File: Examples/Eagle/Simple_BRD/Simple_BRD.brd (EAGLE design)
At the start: 33.7 x 26.7 mm, 6 parts

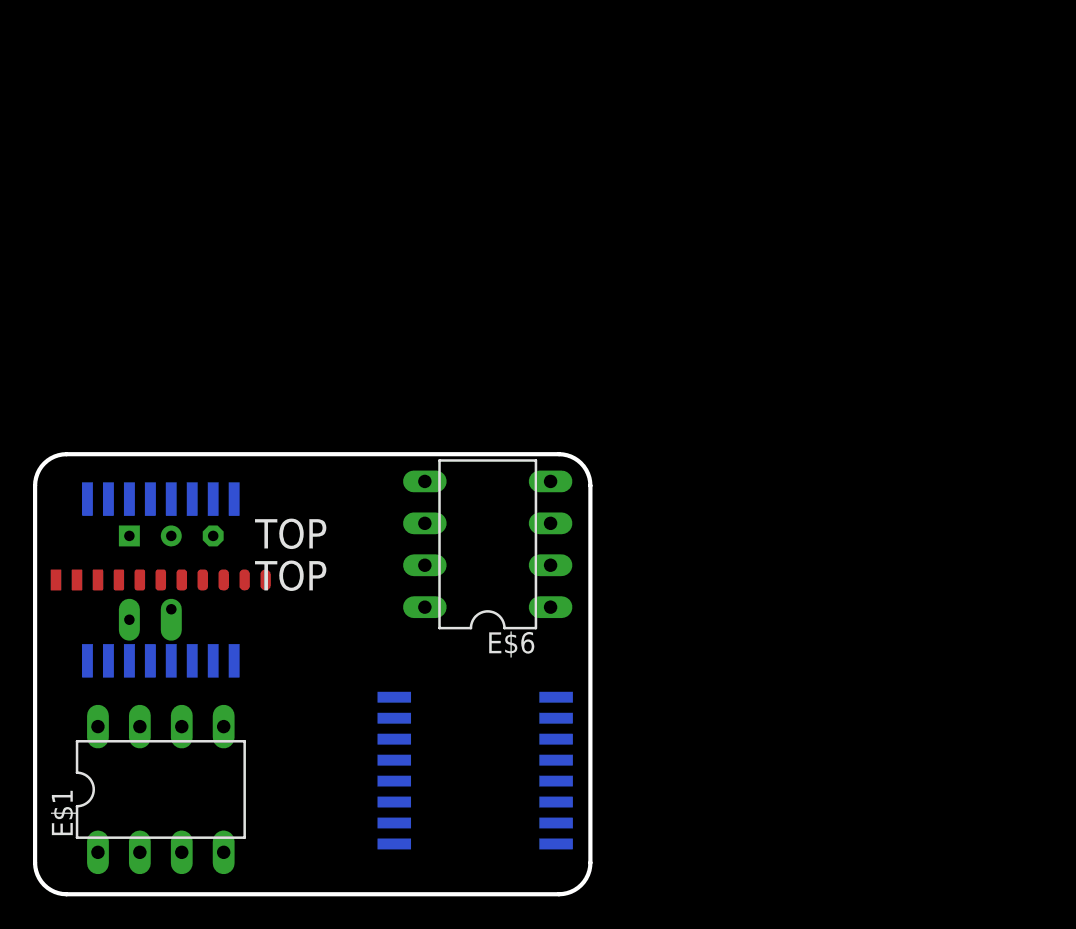
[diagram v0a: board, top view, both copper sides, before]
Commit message: Created new PCB in EagleCAD that utilizes most export features
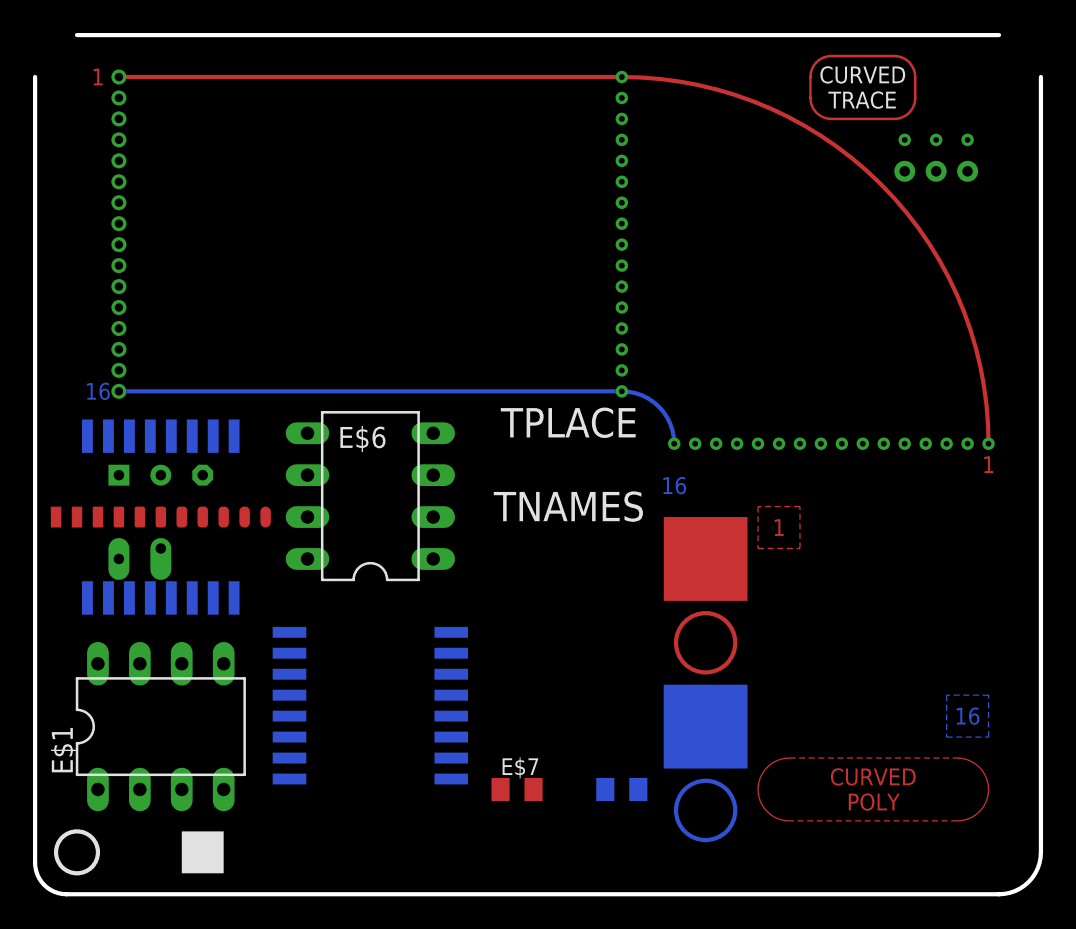
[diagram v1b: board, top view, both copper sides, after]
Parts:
- added E$7, E$8: 1uF, adafruit:C0805K
- moved E$6 7.69 mm to (20.3, 24.1)
- moved E$5 7.47 mm to (20.3, 11.4)
- moved E$1 3.81 mm to (7.62, 10.2)
- moved E$2 3.81 mm to (7.62, 22.9)
- moved E$4 3.81 mm to (7.62, 22.9)
- moved E$3 3.74 mm to (5.08, 25.4)
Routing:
- net S$1: track 0.00 -> 61.9 mm, vias 0 -> 3
- net S$2: track 0.00 -> 60.1 mm, vias 0 -> 3
- net S$4: track 0.00 -> 58.3 mm, vias 0 -> 3
- net S$5: track 0.00 -> 56.5 mm, vias 0 -> 3
- net S$6: track 0.00 -> 54.7 mm, vias 0 -> 3
- net S$7: track 0.00 -> 52.9 mm, vias 0 -> 3
- net S$8: track 0.00 -> 51.1 mm, vias 0 -> 3
- net S$9: track 0.00 -> 49.3 mm, vias 0 -> 3
- net S$10: track 0.00 -> 47.5 mm, vias 0 -> 3
- net S$11: track 0.00 -> 45.7 mm, vias 0 -> 3
- net S$13: track 0.00 -> 44.0 mm, vias 0 -> 3
- net S$12: track 0.00 -> 42.2 mm, vias 0 -> 3
- net S$14: track 0.00 -> 40.4 mm, vias 0 -> 3
- net S$15: track 0.00 -> 38.6 mm, vias 0 -> 3
- net S$16: track 0.00 -> 36.8 mm, vias 0 -> 3
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- added copper zone on layer 1, net TEST
- added copper zone on layer 2, net TEST1
- added copper zone on layer 11, net TEST10
- added copper zone on layer 12, net TEST11
- added copper zone on layer 13, net TEST12
- added copper zone on layer 14, net TEST13
- added copper zone on layer 15, net TEST14
- added copper zone on layer 16, net TEST15
- added copper zone on layer 1, net TEST17
- added copper zone on layer 3, net TEST2
- added copper zone on layer 4, net TEST3
- added copper zone on layer 5, net TEST4
- added copper zone on layer 6, net TEST5
- added copper zone on layer 7, net TEST6
- added copper zone on layer 8, net TEST7
- added copper zone on layer 9, net TEST8
- added copper zone on layer 10, net TEST9
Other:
- board size 33.7 x 26.7 mm -> 61 x 52.1 mm
- board text added: "1"
- board text added: "10"
- board text added: "11"
- board text added: "12"
- board text added: "13"
- board text added: "14"
- board text added: "15"
- board text added: "16"
- board text added: "2"
- board text added: "3"
- board text added: "4"
- board text added: "5"
- board text added: "6"
- board text added: "7"
- board text added: "8"
- board text added: "9"
- board text added: "BDOC"
- board text added: "BNAMES"
- board text added: "BPLACE"
- board text added: "BVALUES"
- board text added: "CURVED POLY"
- board text added: "CURVED TRACE"
- board text added: "TDOC"
- board text added: "TNAMES"
- board text added: "TPLACE"
- board text added: "TVALUES"
- board text removed: "TOP"

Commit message: Updated sample board
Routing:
- net S$24: track 0.00 -> 40.6 mm, vias 0 -> 15
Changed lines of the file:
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@@
 <layer number="25" name="tNames" color="7" fill="1" visible="yes" active="yes"/>
 <layer number="26" name="bNames" color="7" fill="1" visible="yes" active="yes"/>
-<layer number="27" name="tValues" color="7" fill="1" visible="yes" active="yes"/>
-<layer number="28" name="bValues" color="7" fill="1" visible="yes" active="yes"/>
+<layer number="27" name="tValues" color="7" fill="1" visible="no" active="yes"/>
+<layer number="28" name="bValues" color="7" fill="1" visible="no" active="yes"/>
 <layer number="29" name="tStop" color="7" fill="3" visible="no" active="yes"/>
 <layer number="30" name="bStop" color="7" fill="6" visible="no" active="yes"/>
@@
 <text x="52.705" y="10.795" size="1.016" layer="15" font="vector" ratio="15" align="center">15</text>
 <text x="56.515" y="10.795" size="1.016" layer="16" font="vector" ratio="15" align="center">16</text>
-<text x="50.165" y="48.895" size="1.016" layer="21" font="vector" ratio="15" align="center">CURVED
+<text x="48.26" y="49.53" size="1.016" layer="21" font="vector" ratio="15" align="center">CURVED
 TRACE</text>
 <text x="50.8" y="6.35" size="1.016" layer="1" font="vector" ratio="15" align="center">CURVED
@@
 <vertex x="0" y="49.53"/>
 </spline>
+<rectangle x1="17.78" y1="10.16" x2="22.86" y2="15.24" layer="21"/>
+<circle x="20.32" y="6.35" radius="2.83980625" width="0.254" layer="21"/>
 </plain>
 <attributes>
@@
 </signal>
 <signal name="S$3">
-<via x="52.705" y="45.72" extent="1-16" drill="0.35"/>
+<via x="52.705" y="48.26" extent="1-16" drill="0.35"/>
 </signal>
 <signal name="S$18">
-<via x="54.61" y="45.72" extent="1-16" drill="0.35" shape="square"/>
+<via x="55.88" y="48.26" extent="1-16" drill="0.35" shape="square"/>
 </signal>
 <signal name="S$19">
-<via x="56.515" y="45.72" extent="1-16" drill="0.35" shape="octagon"/>
+<via x="59.055" y="48.26" extent="1-16" drill="0.35" shape="octagon"/>
 </signal>
 <signal name="S$20">
-<via x="52.705" y="43.815" extent="1-16" drill="0.635" diameter="1.27"/>
+<via x="52.705" y="46.355" extent="1-16" drill="0.635" diameter="1.27"/>
 </signal>
 <signal name="S$22">
-<via x="54.61" y="43.815" extent="1-16" drill="0.635" diameter="1.27" shape="square"/>
+<via x="55.88" y="46.355" extent="1-16" drill="0.635" diameter="1.27" shape="square"/>
 </signal>
 <signal name="S$23">
-<via x="56.515" y="43.815" extent="1-16" drill="0.635" diameter="1.27" shape="octagon"/>
+<via x="59.055" y="46.355" extent="1-16" drill="0.635" diameter="1.27" shape="octagon"/>
 </signal>
 <signal name="TEST">
@@
 </signal>
 <signal name="S$21">
-<wire x1="52.07" y1="50.8" x2="48.26" y2="50.8" width="0.1524" layer="1"/>
-<wire x1="52.07" y1="50.8" x2="53.34" y2="49.53" width="0.1524" layer="1" curve="-90"/>
-<wire x1="53.34" y1="49.53" x2="53.34" y2="48.26" width="0.1524" layer="1"/>
-<wire x1="48.26" y1="50.8" x2="46.99" y2="49.53" width="0.1524" layer="1" curve="90"/>
-<wire x1="46.99" y1="49.53" x2="46.99" y2="48.26" width="0.1524" layer="1"/>
-<wire x1="46.99" y1="48.26" x2="48.26" y2="46.99" width="0.1524" layer="1" curve="90"/>
-<wire x1="48.26" y1="46.99" x2="52.07" y2="46.99" width="0.1524" layer="1"/>
-<wire x1="52.07" y1="46.99" x2="53.34" y2="48.26" width="0.1524" layer="1" curve="90"/>
+<wire x1="50.165" y1="51.435" x2="46.355" y2="51.435" width="0.1524" layer="1"/>
+<wire x1="50.165" y1="51.435" x2="51.435" y2="50.165" width="0.1524" layer="1" curve="-90"/>
+<wire x1="51.435" y1="50.165" x2="51.435" y2="48.895" width="0.1524" layer="1"/>
+<wire x1="46.355" y1="51.435" x2="45.085" y2="50.165" width="0.1524" layer="1" curve="90"/>
+<wire x1="45.085" y1="50.165" x2="45.085" y2="48.895" width="0.1524" layer="1"/>
+<wire x1="45.085" y1="48.895" x2="46.355" y2="47.625" width="0.1524" layer="1" curve="90"/>
+<wire x1="46.355" y1="47.625" x2="50.165" y2="47.625" width="0.1524" layer="1"/>
+<wire x1="50.165" y1="47.625" x2="51.435" y2="48.895" width="0.1524" layer="1" curve="90"/>
 </signal>
 <signal name="TEST17">
@@
 </polygon>
 </signal>
+<signal name="S$24">
+<wire x1="16.51" y1="1.27" x2="19.05" y2="1.27" width="0.254" layer="1"/>
+<wire x1="19.05" y1="1.27" x2="21.59" y2="1.27" width="0.254" layer="2"/>
+<via x="19.05" y="1.27" extent="1-16" drill="0.508"/>
+<wire x1="21.59" y1="1.27" x2="24.13" y2="1.27" width="0.254" layer="3"/>
+<via x="21.59" y="1.27" extent="1-16" drill="0.508"/>
+<wire x1="24.13" y1="1.27" x2="26.67" y2="1.27" width="0.254" layer="4"/>
+<via x="24.13" y="1.27" extent="1-16" drill="0.508"/>
+<wire x1="26.67" y1="1.27" x2="29.21" y2="1.27" width="0.254" layer="5"/>
+<via x="26.67" y="1.27" extent="1-16" drill="0.508"/>
+<wire x1="29.21" y1="1.27" x2="31.75" y2="1.27" width="0.254" layer="6"/>
+<via x="29.21" y="1.27" extent="1-16" drill="0.508" shape="square"/>
+<wire x1="31.75" y1="1.27" x2="34.29" y2="1.27" width="0.254" layer="7"/>
+<via x="31.75" y="1.27" extent="1-16" drill="0.508" shape="square"/>
+<wire x1="34.29" y1="1.27" x2="36.83" y2="1.27" width="0.254" layer="8"/>
+<via x="34.29" y="1.27" extent="1-16" drill="0.508" shape="square"/>
+<wire x1="36.83" y1="1.27" x2="39.37" y2="1.27" width="0.254" layer="9"/>
+<via x="36.83" y="1.27" extent="1-16" drill="0.508" shape="square"/>
+<wire x1="39.37" y1="1.27" x2="41.91" y2="1.27" width="0.254" layer="10"/>
+<via x="39.37" y="1.27" extent="1-16" drill="0.508" shape="octagon"/>
+<wire x1="41.91" y1="1.27" x2="44.45" y2="1.27" width="0.254" layer="11"/>
+<via x="41.91" y="1.27" extent="1-16" drill="0.508" shape="octagon"/>
+<wire x1="44.45" y1="1.27" x2="46.99" y2="1.27" width="0.254" layer="12"/>
+<via x="44.45" y="1.27" extent="1-16" drill="0.508" shape="octagon"/>
+<wire x1="46.99" y1="1.27" x2="49.53" y2="1.27" width="0.254" layer="13"/>
+<via x="46.99" y="1.27" extent="1-16" drill="0.508" shape="octagon"/>
+<wire x1="49.53" y1="1.27" x2="52.07" y2="1.27" width="0.254" layer="14"/>
+<via x="49.53" y="1.27" extent="1-16" drill="0.508"/>
+<wire x1="52.07" y1="1.27" x2="54.61" y2="1.27" width="0.254" layer="15"/>
+<via x="52.07" y="1.27" extent="1-16" drill="0.508" shape="square"/>
+<wire x1="54.61" y1="1.27" x2="57.15" y2="1.27" width="0.254" layer="16"/>
+<via x="54.61" y="1.27" extent="1-16" drill="0.508" shape="octagon"/>
+</signal>
+<signal name="S$25">
+<via x="52.705" y="43.815" extent="1-16" drill="1.27" diameter="2.54"/>
+</signal>
+<signal name="S$26">
+<via x="55.88" y="43.815" extent="1-16" drill="1.27" diameter="2.54" shape="square"/>
+</signal>
+<signal name="S$27">
+<via x="59.055" y="43.815" extent="1-16" drill="1.27" diameter="2.54" shape="octagon"/>
+</signal>
 </signals>
